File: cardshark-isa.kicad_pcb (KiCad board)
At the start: 4 copper layers, 153.5 x 82.1 mm, 100 parts, among them J1 Conn_02x13_Odd_Even, J3 DE15_Receptacle_HighDensity_M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, J4 Bus_ISA_16bit, U1 GD543x_ISA, U11 93CxxA, U12 SOJ_256Kx16, U13 SOJ_256Kx16, U2 27C256, U3 SOJ_256Kx16, U5 74AHCT1G04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

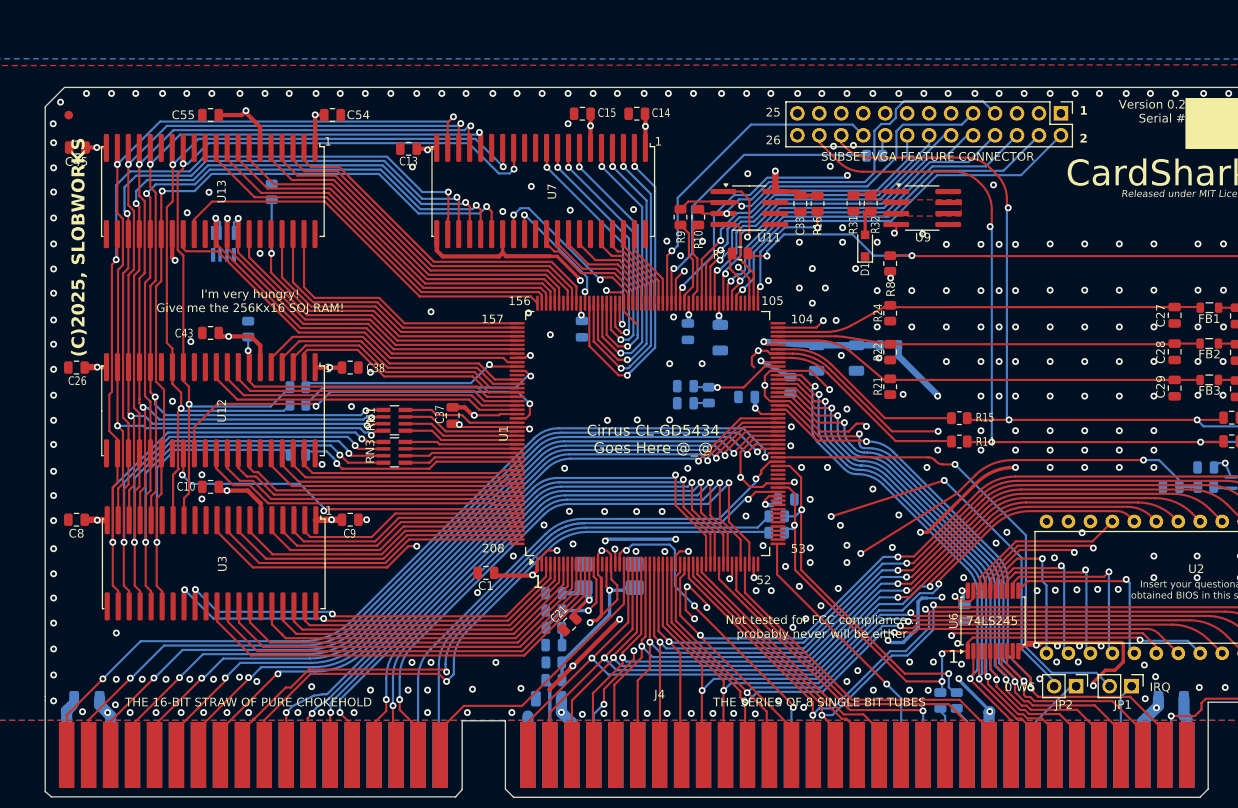
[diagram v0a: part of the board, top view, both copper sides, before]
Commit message: Add files via upload
Uploaded wrong version of board files by mistake; uploaded correct working version this time
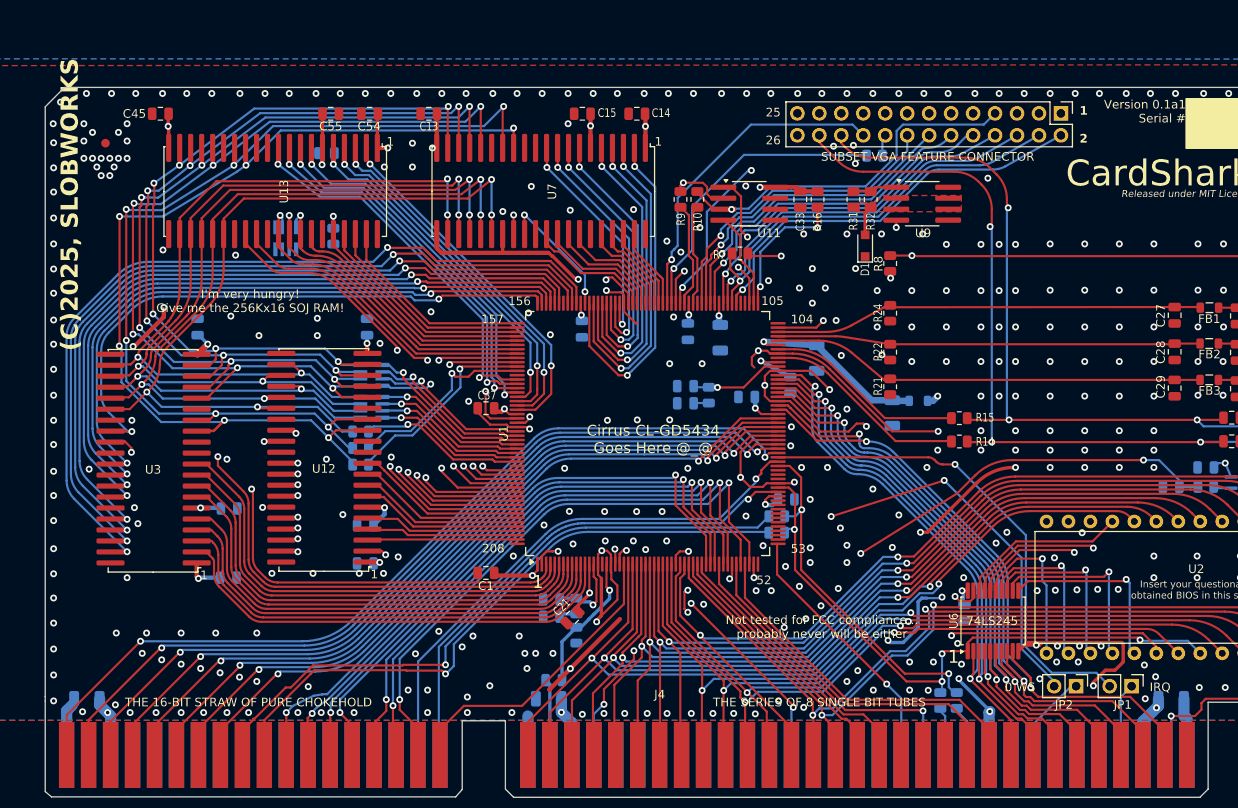
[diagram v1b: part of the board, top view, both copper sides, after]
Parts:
- removed C18: 0.22u, Capacitor_SMD:C_0805_2012Metric
- removed Y1: 14.31818MHz, Crystal:Crystal_SMD_7050-4Pin_7.0x5.0mm
- C10, C26, C38, C43, C8, C9, RN1, RN3: moved to B.Cu
- moved C26 33.9 mm to (159.0, 86.0), turned to -90 degrees
- moved C43 28.6 mm to (158.8, 109.0)
- moved C8 26.3 mm to (139.4, 86.0), turned to -90 degrees
- moved C38 22.7 mm to (158.8, 113.3), turned to 0 degrees
- moved R3 22.3 mm to (154.3, 65.9), turned to 0 degrees
- moved C9 15.6 mm to (142.9, 115.0)
- moved U12 14.2 mm to (154.0, 101.0), turned to 180 degrees
- moved U3 14.0 mm to (134.2, 101.1), turned to 180 degrees
- moved C55 13.9 mm to (154.8, 61.3), turned to 180 degrees
- moved R6 11.5 mm to (158.2, 101.9)
- moved C45 10.4 mm to (135.1, 61.3)
- moved R2 8.81 mm to (158.2, 100.0)
- moved R1 8.78 mm to (155.1, 75.5), turned to 90 degrees
- moved R4 7.74 mm to (158.2, 98.1)
- moved C17 7.59 mm to (219.8, 96.0)
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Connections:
- RN3 pad 5: /MA4 -> /MA7
- RN3 pad 6: /MA5 -> /MA6
- RN3 pad 7: /MA6 -> /MA5
- RN3 pad 8: /MA7 -> /MA4
- U1 pad 185: Net-(RN3-R4.1) -> Net-(RN3-R1.1)
- U1 pad 186: Net-(RN3-R3.1) -> Net-(RN3-R2.1)
- U1 pad 187: Net-(RN3-R2.1) -> Net-(RN3-R3.1)
- U1 pad 188: Net-(RN3-R1.1) -> Net-(RN3-R4.1)
- U12 pad 10: /MD48 -> /MD39
- U12 pad 2: /MD52 -> /MD32
- U12 pad 29: /CAS6 -> /CAS4
- U12 pad 3: /MD53 -> /MD33
- U12 pad 4: /MD54 -> /MD34
- U12 pad 5: /MD55 -> /MD35
- U12 pad 7: /MD51 -> /MD36
- U12 pad 8: /MD50 -> /MD37
- U12 pad 9: /MD49 -> /MD38
- U13 pad 10: /MD8 -> /MD55
- U13 pad 2: /MD15 -> /MD48
- U13 pad 29: /CAS1 -> /CAS6
- U13 pad 3: /MD14 -> /MD49
- U13 pad 4: /MD13 -> /MD50
- U13 pad 5: /MD12 -> /MD51
- U13 pad 7: /MD11 -> /MD52
- U13 pad 8: /MD10 -> /MD53
- U13 pad 9: /MD9 -> /MD54
- U3 pad 10: /MD32 -> /MD7
- U3 pad 2: /MD39 -> /MD0
- U3 pad 28: /CAS0 -> /CAS1
- U3 pad 29: /CAS4 -> /CAS0
- U3 pad 3: /MD38 -> /MD1
- U3 pad 31: /MD0 -> /MD8
- U3 pad 32: /MD1 -> /MD9
- U3 pad 33: /MD2 -> /MD10
- U3 pad 34: /MD3 -> /MD11
- U3 pad 36: /MD4 -> /MD12
- U3 pad 37: /MD5 -> /MD13
- U3 pad 38: /MD6 -> /MD14
- U3 pad 39: /MD7 -> /MD15
- U3 pad 4: /MD37 -> /MD2
- U3 pad 5: /MD36 -> /MD3
- U3 pad 7: /MD35 -> /MD4
- U3 pad 8: /MD34 -> /MD5
- U3 pad 9: /MD33 -> /MD6
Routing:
- net /MD15: track 40.9 -> 98.4 mm, vias 0 -> 2
- net /MD14: track 41.5 -> 95.1 mm, vias 0 -> 2
- net /MA4: track 140.0 -> 89.5 mm
- net /MD13: track 42.2 -> 91.7 mm, vias 0 -> 2
- net /MD12: track 42.6 -> 88.2 mm, vias 0 -> 2
- net /MA5: track 135.4 -> 90.5 mm
- net /MA6: track 133.4 -> 93.5 mm
- net /MA7: track 131.5 -> 94.1 mm
- net /MD11: track 44.5 -> 81.8 mm, vias 0 -> 2
- net /MD10: track 45.1 -> 80.0 mm, vias 0 -> 2
- net /MD9: track 45.7 -> 76.8 mm, vias 0 -> 2
- net /MA3: track 120.5 -> 92.9 mm, vias 4 -> 6
- net /MD8: track 46.4 -> 73.9 mm, vias 0 -> 2
- net /VCC: track 183.5 -> 160.9 mm
- net /CAS1: track 47.1 -> 69.4 mm, vias 0 -> 2
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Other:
- board text added: "Version 0.1a1 Serial #"
- board text added: "i don't do what you do i don't think what you think i am not you"
- board text removed: "4-pin Osc: Y1, C18 Bus Osc: C5, R20 ~{Do NOT fit both} at same time."
- board text removed: "Version 0.2 Serial #"

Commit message: Add files via upload
Uploaded CSV BOM. Made various little, very minor quick fixes, mostly of a cosmetic nature.
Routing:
- net GND: track 257.1 -> 252.4 mm
- net /SD6: track 70.0 -> 69.2 mm
- net /SD5: track 67.7 -> 67.0 mm
- net /SD4: track 65.4 -> 64.7 mm
- net /VFILTER: track 10.8 -> 10.3 mm
